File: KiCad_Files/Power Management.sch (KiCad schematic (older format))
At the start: 24 parts, among them IC1 TLV809ED29DBZR, IC2 MAX17201G+T, IC4 TC1264-3.3VDB, Q4 Q_PMOS_GSD, U2 TPS61092

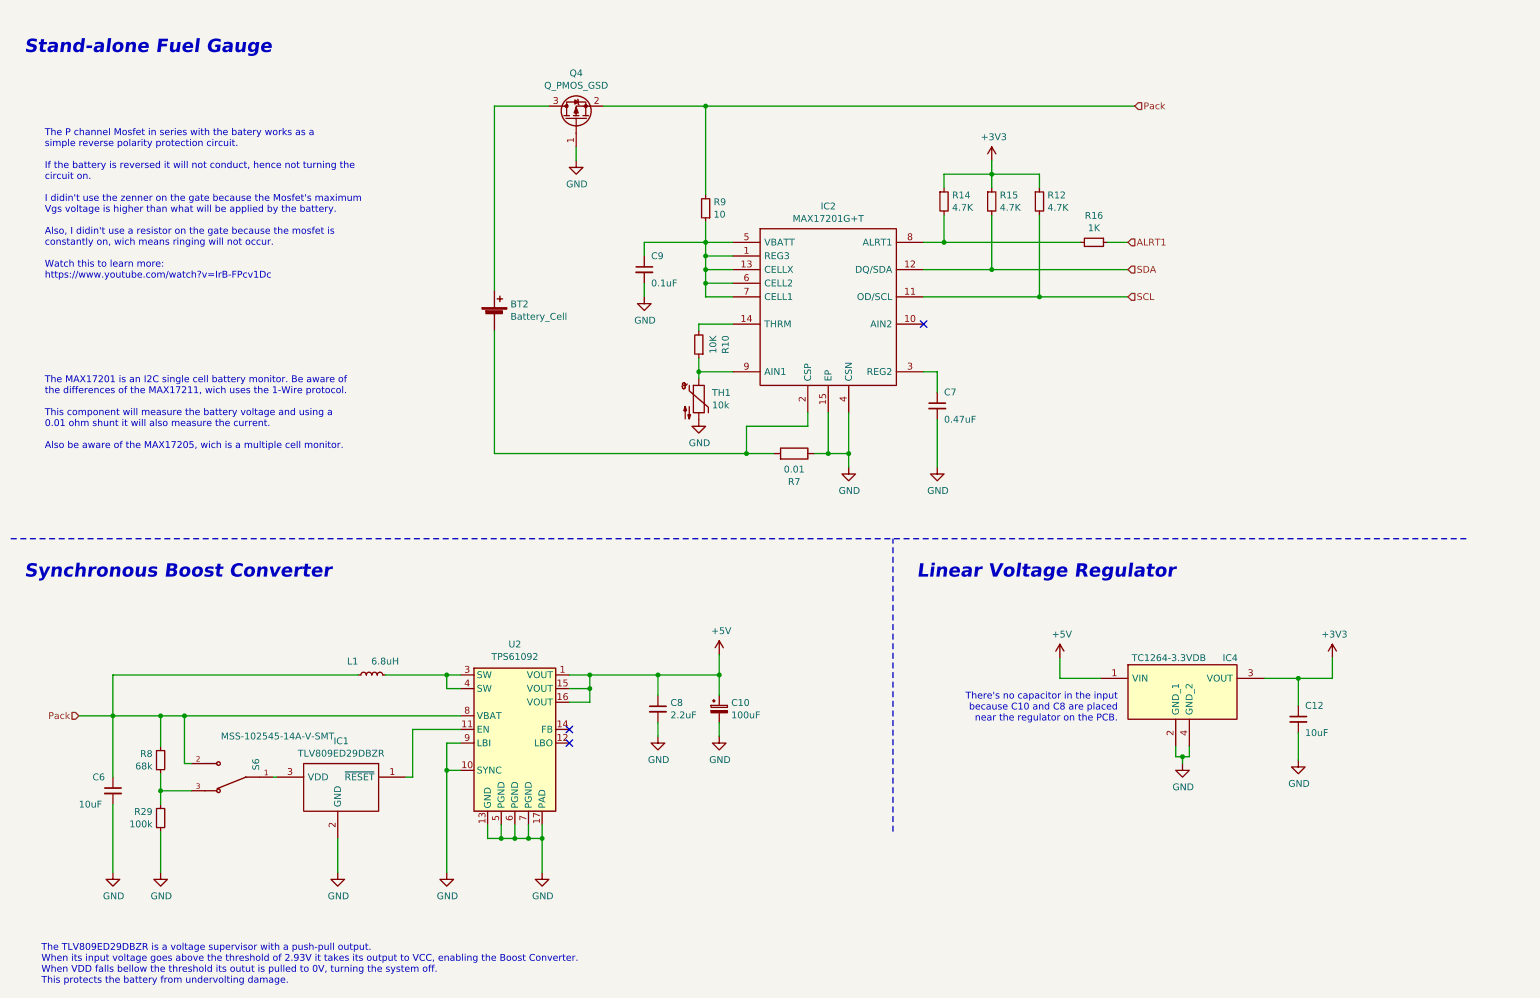
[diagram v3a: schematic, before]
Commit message: Add MS5607 barometer.
Adds MS5607 barometer and reorganized silkscreen.
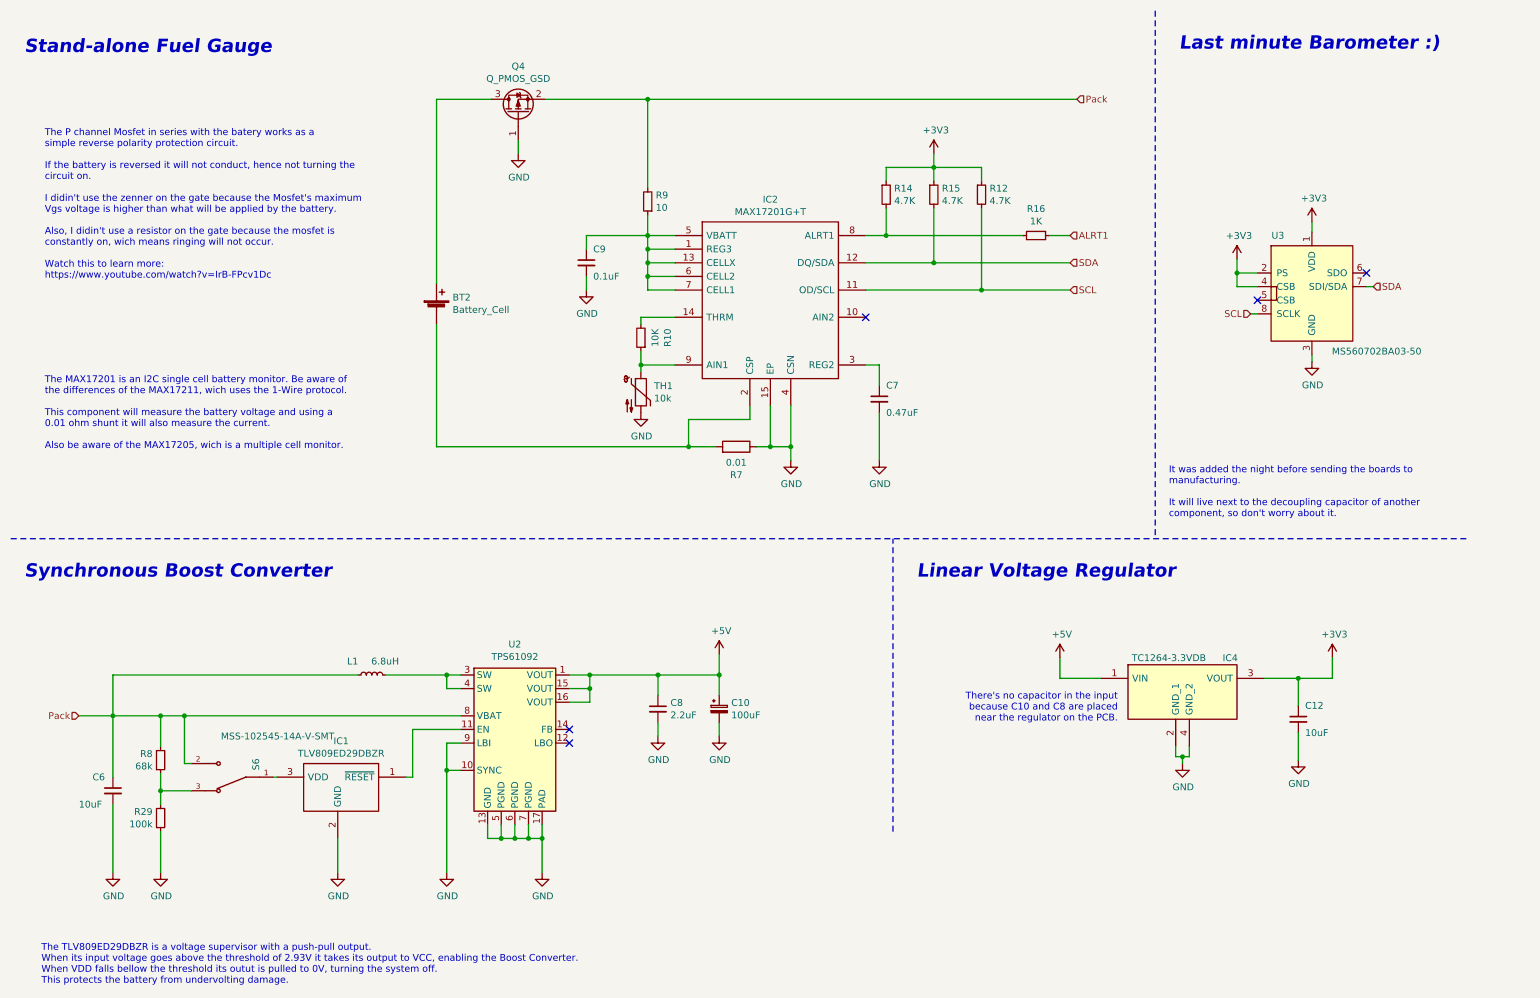
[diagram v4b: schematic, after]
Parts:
- added U3: MS560702BA03-50, digikey-footprints:SMD-8_5x3mm, symbol dk_Pressure-Sensors-Transducers:MS560702BA03-50
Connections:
- net +3V3: now also U3.1 (VDD), U3.2 (PS), U3.4 (CSB)
- net GND: now also U3.3 (GND)
- net SCL: now also U3.8 (SCLK)
- net SDA: now also U3.7 (SDI/SDA)
- no-connect marks 3 -> 5
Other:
- note added: "It was added the night before sending the boards to\nmanufacturing.\n\nIt will live next to the decoupling capacitor of another\ncomponent, so don't worry about it."
- note added: "Last minute Barometer :)"
- moved on the sheet: BT2, C7, C9, IC2, Q4, R10, R12, R14, R15, R16, R7, R9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
